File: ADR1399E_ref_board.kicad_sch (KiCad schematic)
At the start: 106 parts, among them IC1 ADP7118ARDZ-R7, J1 Conn_01x02_Pin, J2 USB_C_Receptacle_PowerOnly_6P, J3 Conn_Coaxial, J4 S4B-XH-A, P1 JST_B2P_VH, Q1 MMBT3906, U2 TPS61085DGK, U3 OPA182IDR, U4 OPA994IDR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

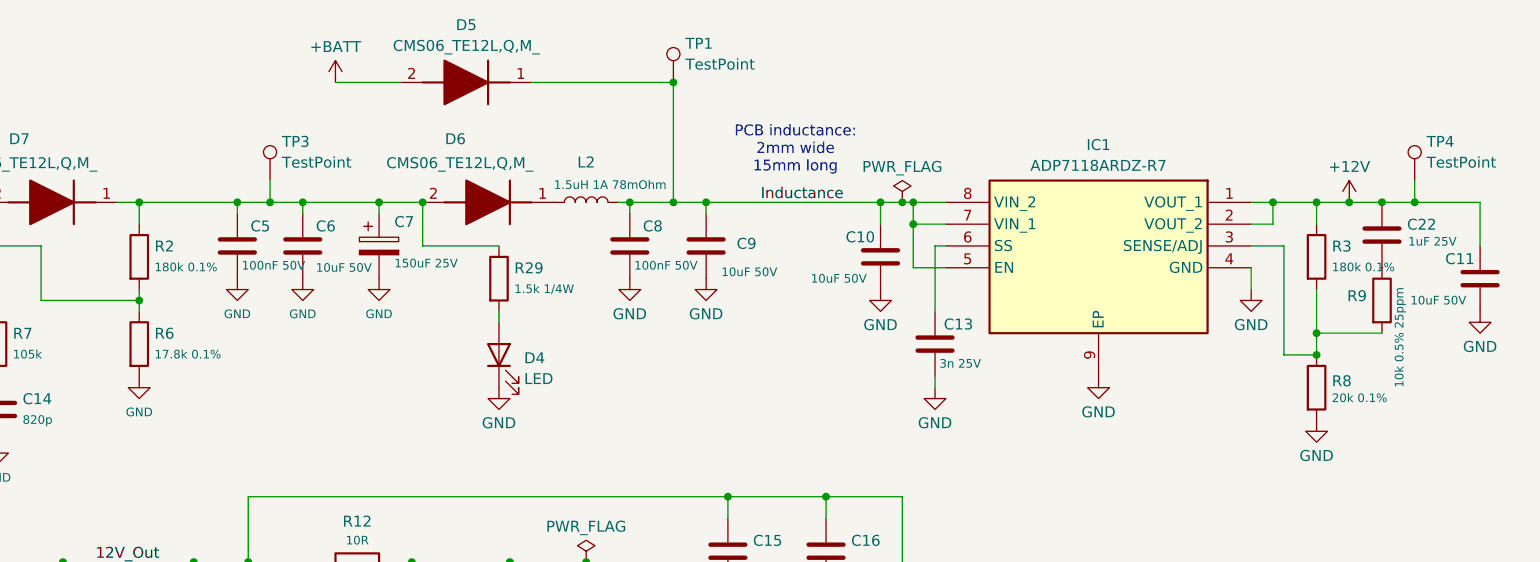
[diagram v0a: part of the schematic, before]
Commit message: changed to 15V, adp7142
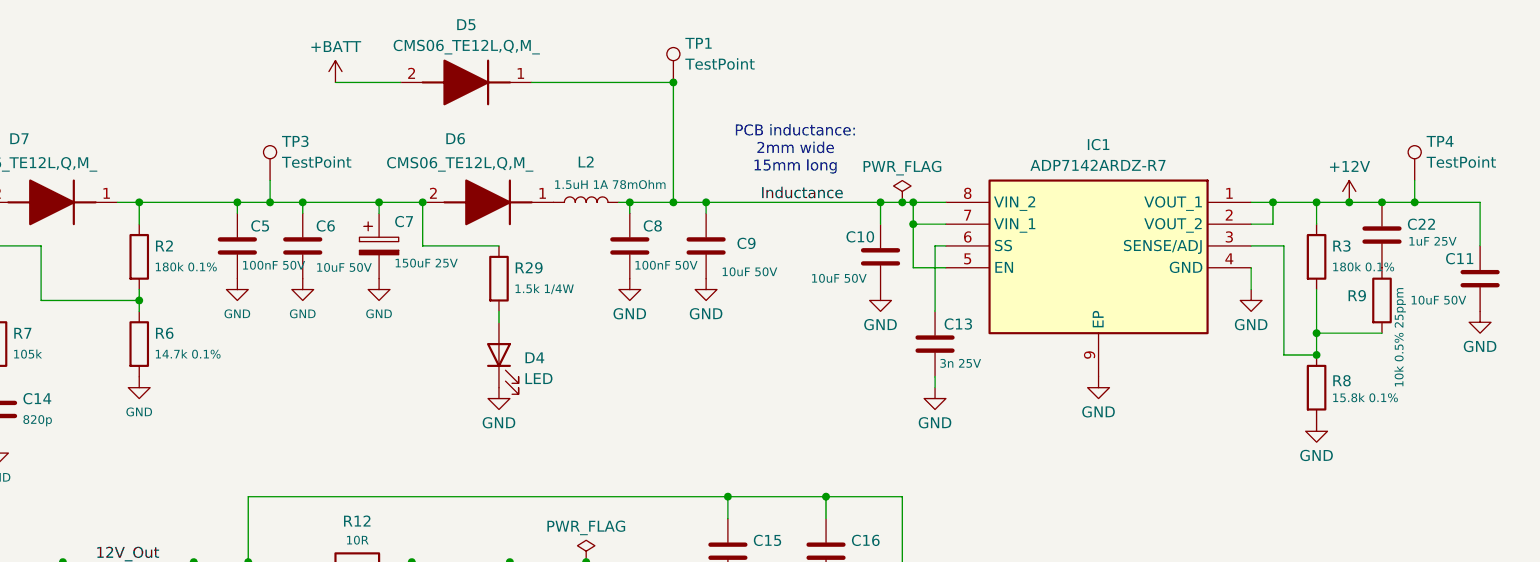
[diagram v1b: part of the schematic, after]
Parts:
- IC1: value ADP7118ARDZ-R7 -> ADP7142ARDZ-R7; Manufacturer_Part_Number ADP7118ARDZ-R7 -> ADP7142ARDZ-R7
- R6: value 17.8k 0.1% -> 14.7k 0.1%
- R8: value 20k 0.1% -> 15.8k 0.1%
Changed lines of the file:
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@@
 			)
 		)
-		(property "Value" "17.8k 0.1%"
+		(property "Value" "14.7k 0.1%"
 			(at 127.508 69.7921 0)
 			(effects
@@
 			)
 		)
-		(property "Value" "20k 0.1%"
+		(property "Value" "15.8k 0.1%"
 			(at 264.668 74.8721 0)
 			(effects
@@
 			)
 		)
-		(property "Value" "ADP7118ARDZ-R7"
+		(property "Value" "ADP7142ARDZ-R7"
 			(at 237.49 47.8098 0)
 			(effects
@@
 			)
 		)
-		(property "Manufacturer_Part_Number" "ADP7118ARDZ-R7"
+		(property "Manufacturer_Part_Number" "ADP7142ARDZ-R7"
 			(at 223.52 846.99 0)
 			(effects

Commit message: cleanup
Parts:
- R24: value 180k 0.1% -> 120k 0.1%
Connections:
- net +12V renamed +15V
- net 12V_Out renamed 15V_Out
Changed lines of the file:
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@@
 		)
 	)
+	(text_box "Tighter values need to be claculated"
+		(exclude_from_sim no)
+		(at 19.05 83.82 0)
+		(size 54.61 46.99)
+		(margins 0.9525 0.9525 0.9525 0.9525)
+		(stroke
+			(width 0)
+			(type solid)
+		)
+		(fill
+			(type none)
+		)
+		(effects
+			(font
+				(size 1.27 1.27)
+			)
+			(justify left top)
+		)
+	)
 	(text_box "To Be placed over RN1"
 		(exclude_from_sim no)
@@
 		)
 	)
-	(label "12V_Out"
+	(label "15V_Out"
 		(at 120.65 93.98 0)
 		(effects
@@
 			)
 		)
-		(property "Value" "+12V"
+		(property "Value" "+15V"
 			(at 266.7 47.9369 0)
 			(effects
@@
 			)
 		)
-		(property "Value" "+12V"
+		(property "Value" "+15V"
 			(at 85.09 83.4969 0)
 			(effects
@@
 			)
 		)
-		(property "Value" "180k 0.1%"
+		(property "Value" "120k 0.1%"
 			(at 27.178 128.2121 0)
 			(effects

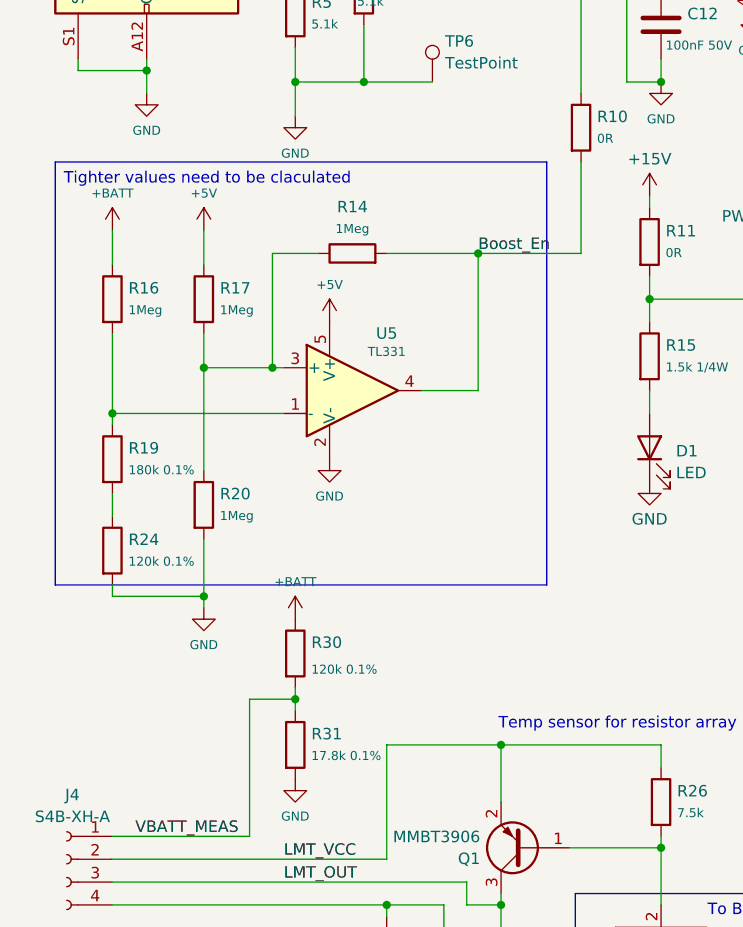
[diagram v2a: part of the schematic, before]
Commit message: Replaced Boost enable comparator with N-MOS
also changed Vbatt divider resistor value
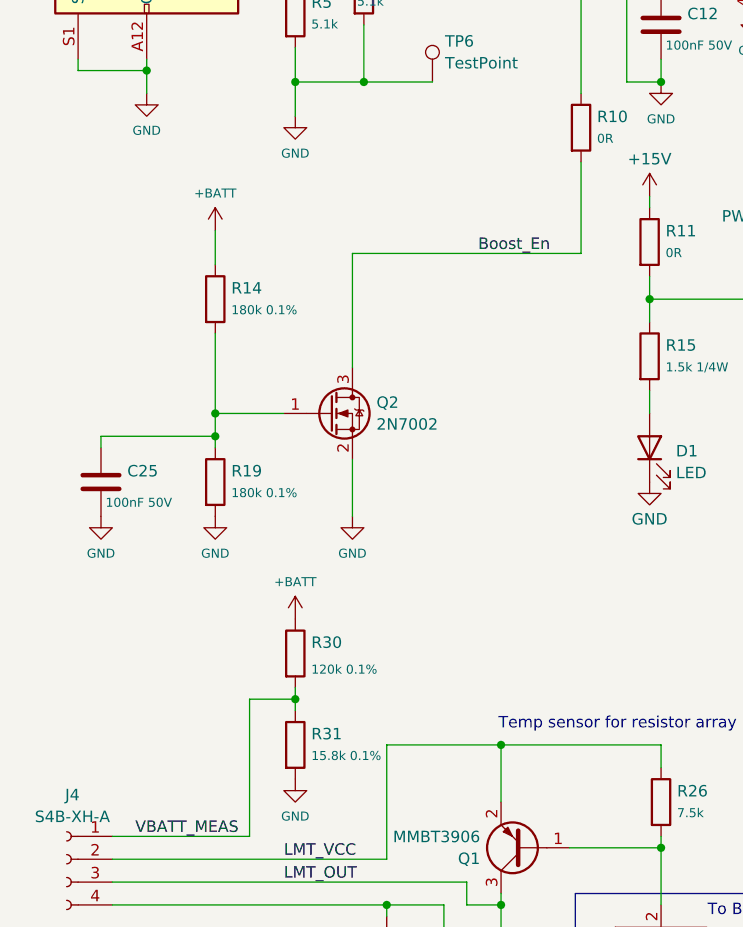
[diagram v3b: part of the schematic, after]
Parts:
- removed R16, R17, R20: 1Meg, Resistor_SMD:R_0603_1608Metric_Pad0.98x0.95mm_HandSolder, symbol Device:R
- removed R24: 120k 0.1%, Resistor_SMD:R_0603_1608Metric_Pad0.98x0.95mm_HandSolder, symbol Device:R
- removed U5: TL331, Package_TO_SOT_SMD:SOT-23-5, symbol Comparator:TL331
- added C25: 100nF 50V, Capacitor_SMD:C_0603_1608Metric_Pad1.08x0.95mm_HandSolder, symbol Device:C
- added Q2: 2N7002, Package_TO_SOT_SMD:SOT-23, symbol Transistor_FET:2N7002
- R14: value 1Meg -> 180k 0.1%; Manufacturer_Name KOA Speer -> Panasonic; Manufacturer_Part_Number RN73R1JTTD1004B25 -> ERA-3AEB184V
- R31: value 17.8k 0.1% -> 15.8k 0.1%
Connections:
- net +BATT: now also R14.1
- net Boost_En: now also Q2.3 (D); no longer R14.2
- net GND: now also R19.2, C25.2, Q2.2 (S)
- net at R19.1: now also R14.2, C25.1, Q2.1 (G)
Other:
- moved on the sheet: R19
